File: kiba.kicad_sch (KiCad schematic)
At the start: 10 parts, among them J1 Raspberry_Pi_2_3, J2 Conn_01x02, Q1 2N7002NXAKR, U1 LM1117MP-3.3

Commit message: fix: missing footprints
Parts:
- J1: footprint (none) -> Local:raspberrypi
- J2: footprint (none) -> Connector_PinHeader_2.54mm:PinHeader_1x02_P2.54mm_Vertical
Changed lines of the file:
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@@
 			)
 		)
-		(property "Footprint" ""
+		(property "Footprint" "Connector_PinHeader_2.54mm:PinHeader_1x02_P2.54mm_Vertical"
 			(at 214.63 128.27 0)
 			(effects
@@
 			)
 		)
-		(property "Footprint" ""
+		(property "Footprint" "Local:raspberrypi"
 			(at 95.25 102.87 0)
 			(effects

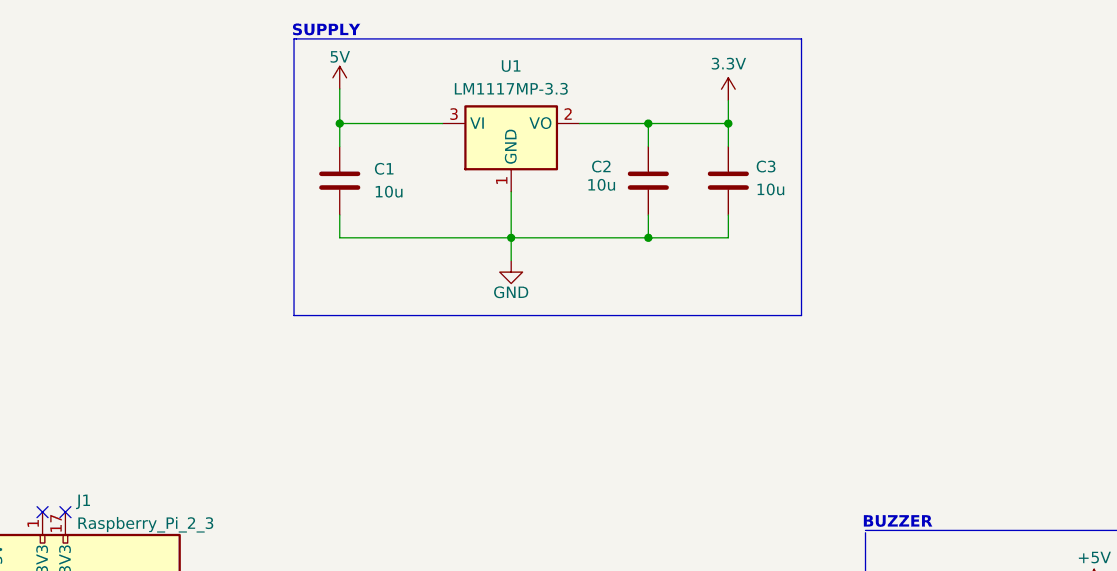
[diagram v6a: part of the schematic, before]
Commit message: fix: missing save and add leds + fuse on power supply
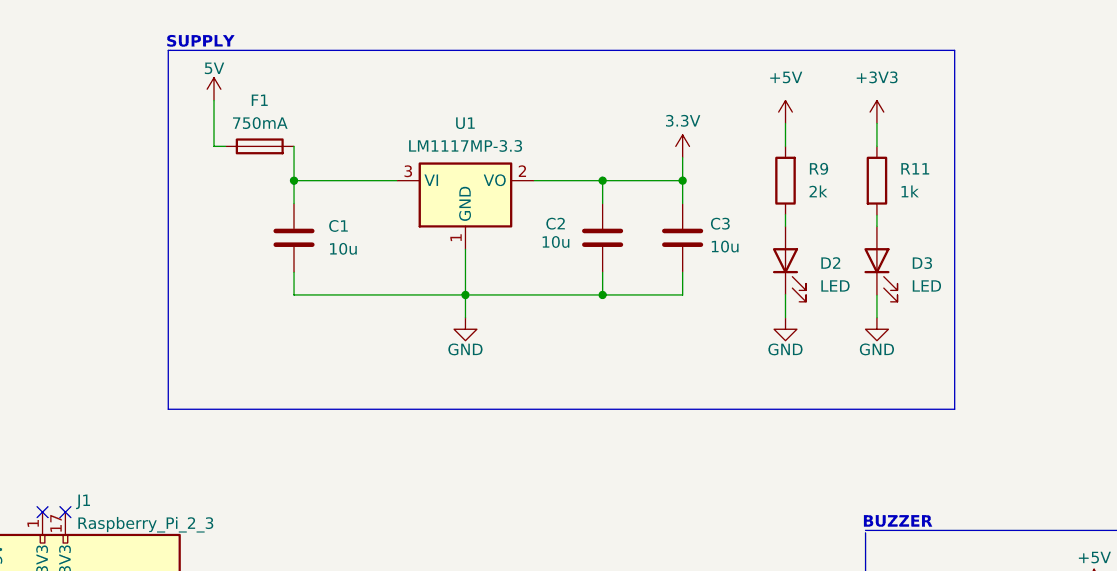
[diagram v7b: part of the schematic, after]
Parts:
- added D2, D3: LED, symbol Device:LED
- added F1: 750mA, symbol Device:Fuse
- added R11: 1k, symbol Device:R
- added R9: 2k, symbol Device:R
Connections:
- net +5V: now also R9.2
- net 5V: now also F1.1; no longer C1.1, U1.3 (VI)
- net GND: now also D2.1 (K), D3.1 (K)
- new net: D3.2 (A), R11.2
- new net: C1.1, F1.2, U1.3 (VI)
- new net: D2.2 (A), R9.1
- new net +3V3: R11.1
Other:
- moved on the sheet: C1, C2, C3, U1

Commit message: fix: missing footprints
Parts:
- D2, D3: footprint (none) -> Diode_SMD:D_0603_1608Metric
- F1: footprint (none) -> Fuse:Fuse_0603_1608Metric
- R11, R9: footprint (none) -> Resistor_SMD:R_0603_1608Metric
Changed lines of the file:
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@@
 			)
 		)
-		(property "Footprint" ""
+		(property "Footprint" "Diode_SMD:D_0603_1608Metric"
 			(at 190.5 41.91 0)
 			(effects
@@
 			)
 		)
-		(property "Footprint" ""
+		(property "Footprint" "Fuse:Fuse_0603_1608Metric"
 			(at 121.92 30.988 90)
 			(effects
@@
 			)
 		)
-		(property "Footprint" ""
+		(property "Footprint" "Resistor_SMD:R_0603_1608Metric"
 			(at 188.722 33.02 90)
 			(effects
@@
 			)
 		)
-		(property "Footprint" ""
+		(property "Footprint" "Resistor_SMD:R_0603_1608Metric"
 			(at 182.118 33.02 90)
 			(effects
@@
 			)
 		)
-		(property "Footprint" ""
+		(property "Footprint" "Diode_SMD:D_0603_1608Metric"
 			(at 180.34 41.91 0)
 			(effects
